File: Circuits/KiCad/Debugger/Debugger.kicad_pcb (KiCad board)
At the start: 2 copper layers, 104.1 x 104.1 mm, 11 parts, among them J1 BUS1, J2 BUS2, SW1 RESET, SW2 POWER

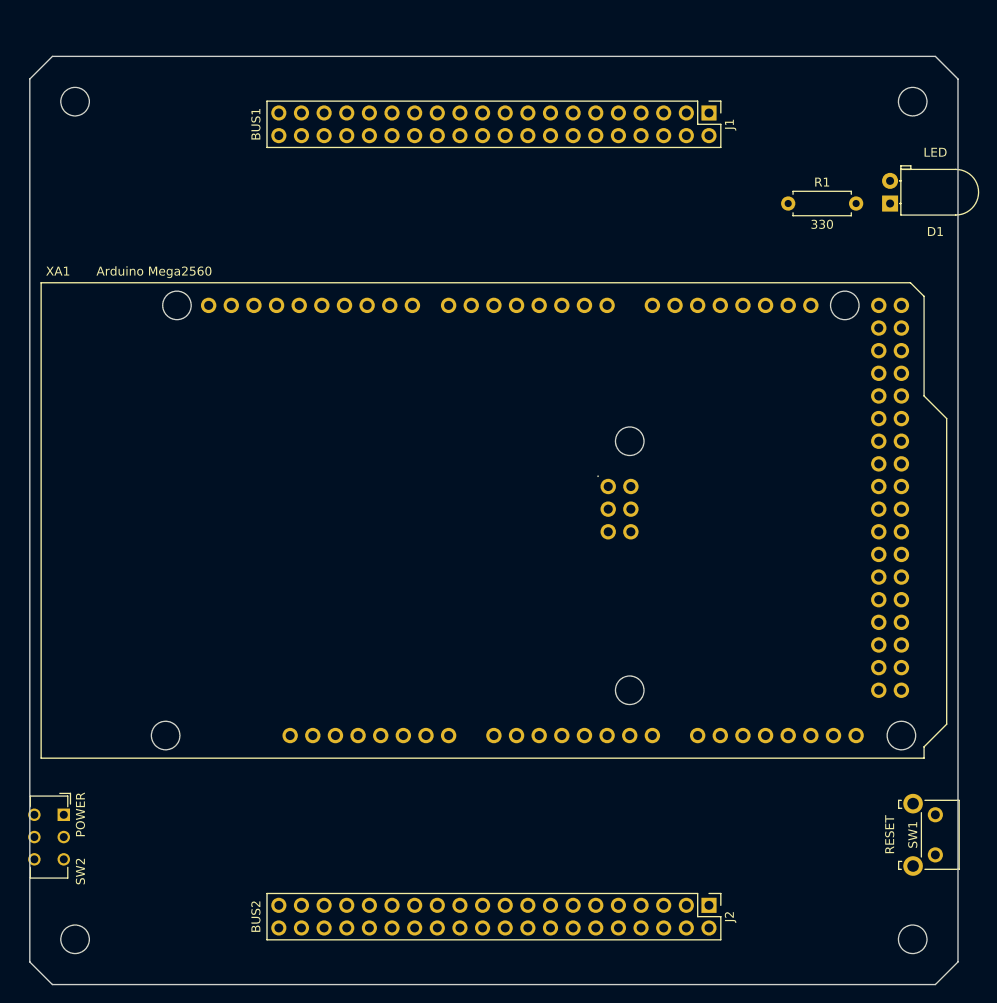
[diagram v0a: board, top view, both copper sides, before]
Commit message: Updated PCB for Bottom and Debugger (sent to manufacturer)
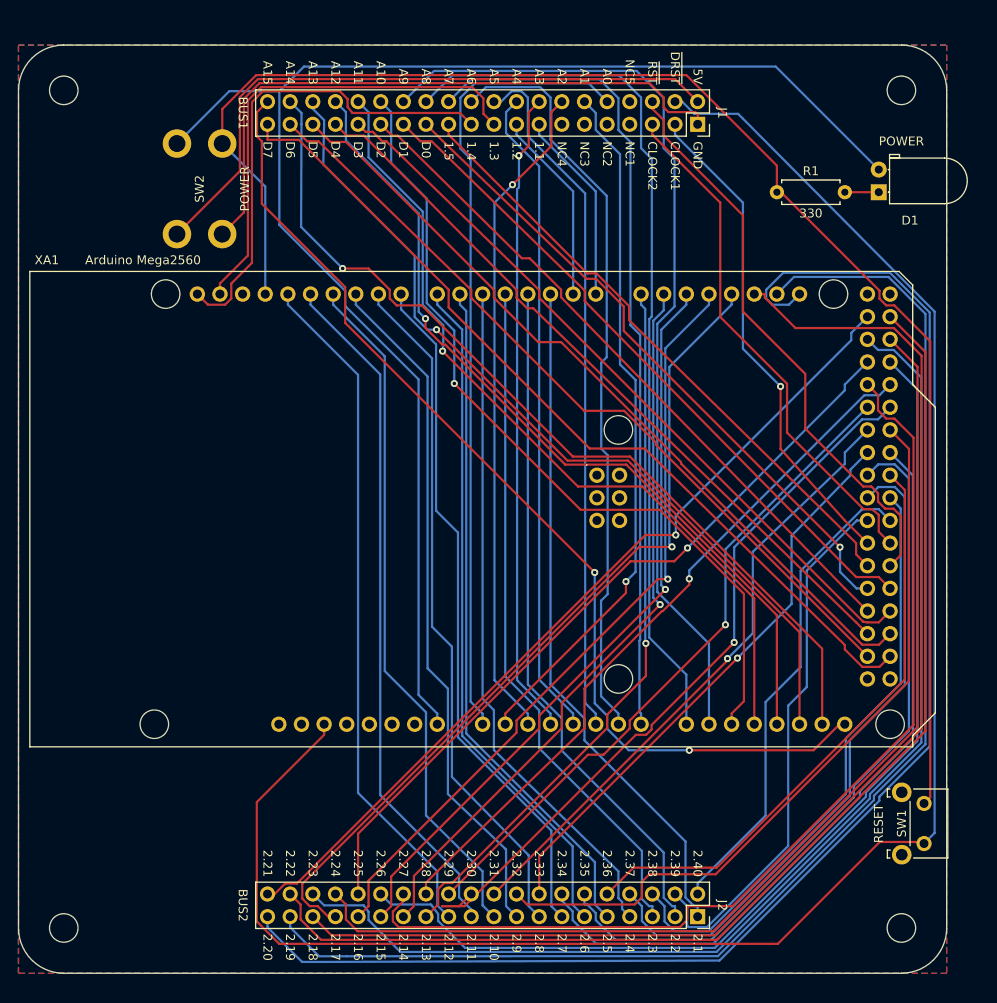
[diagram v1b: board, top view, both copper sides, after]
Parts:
- D1: value LED -> POWER
- J1, J2: footprint Connector_PinHeader_2.54mm:PinHeader_2x20_P2.54mm_Vertical -> Connector_PinSocket_2.54mm:PinSocket_2x20_P2.54mm_Vertical
- SW2: footprint Button_Switch_THT:SW_CuK_JS202011AQN_DPDT_Angled -> DM-02:Switch_DPST_Angled
- moved SW2 62.9 mm to (39.4, 49.5), turned to 90 degrees
- moved H3 1.80 mm to (124.5, 124.5)
- moved SW1 1.80 mm to (127.0, 110.5)
- moved R1 1.80 mm to (110.5, 41.9)
- moved H2 1.80 mm to (30.5, 124.5)
- moved H4 1.80 mm to (124.5, 30.5)
- moved J1 1.80 mm to (101.6, 34.3)
- moved J2 1.80 mm to (101.6, 123.2)
- moved D1 1.80 mm to (121.9, 41.9)
- moved H1 1.80 mm to (30.5, 30.5)
- moved XA1 1.80 mm to (26.7, 104.1)
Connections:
- D1 pad 2: COMPUTER_5V -> ARDUINO_5V
- J1 pad 15: Net-(J1-Pad15) -> BUS1_1
- J1 pad 17: Net-(J1-Pad17) -> BUS1_2
- J1 pad 19: Net-(J1-Pad19) -> BUS1_3
- J1 pad 21: Net-(J1-Pad21) -> BUS1_4
- J1 pad 23: Net-(J1-Pad23) -> BUS1_5
- J1 pad 3: Net-(J1-Pad3) -> CLOCK1
- J1 pad 5: Net-(J1-Pad5) -> CLOCK2
- XA1 pad D0: Net-(XA1-PadD0) -> BUS1_1
- XA1 pad D1: Net-(XA1-PadD1) -> BUS1_2
- XA1 pad D42: Net-(XA1-PadD42) -> CLOCK1
- XA1 pad D43: Net-(XA1-PadD43) -> CLOCK2
- XA1 pad D44: Net-(XA1-PadD44) -> BUS1_5
- XA1 pad SCL: Net-(XA1-PadSCL) -> BUS1_4
- XA1 pad SDA: Net-(XA1-PadSDA) -> BUS1_3
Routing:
- net ~DEBUG_RESET: track 0.00 -> 205.1 mm
- net ARDUINO_GND: track 0.00 -> 170.5 mm
- net ARDUINO_5V: track 0.00 -> 165.5 mm
- net BUS2_20: track 0.00 -> 162.5 mm
- net BUS2_19: track 0.00 -> 151.4 mm
- net BUS2_18: track 0.00 -> 142.5 mm
- net BUS2_22: track 0.00 -> 132.2 mm
- net BUS2_23: track 0.00 -> 130.4 mm
- net BUS2_24: track 0.00 -> 122.3 mm
- net BUS2_26: track 0.00 -> 116.9 mm
- net A15: track 0.00 -> 116.8 mm, vias 0 -> 2
- net BUS2_27: track 0.00 -> 113.3 mm
- net A9: track 0.00 -> 105.9 mm
- net A14: track 0.00 -> 101.7 mm, vias 0 -> 1
- net A8: track 0.00 -> 99.1 mm
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- added copper zone on B.Cu, net (none)
- added copper zone on F.Cu, net (none)
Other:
- outline, holes or cut-outs redrawn
- board text added: "1.1"
- board text added: "1.2"
- board text added: "1.3"
- board text added: "1.4"
- board text added: "1.5"
- board text added: "2.1"
- board text added: "2.10"
- board text added: "2.11"
- board text added: "2.12"
- board text added: "2.13"
- board text added: "2.14"
- board text added: "2.15"
- board text added: "2.16"
- board text added: "2.17"
- board text added: "2.18"
- board text added: "2.19"
- board text added: "2.2"
- board text added: "2.20"
- board text added: "2.21"
- board text added: "2.22"
- board text added: "2.23"
- board text added: "2.24"
- board text added: "2.25"
- board text added: "2.26"
- board text added: "2.27"
- board text added: "2.28"
- board text added: "2.29"
- board text added: "2.3"
- board text added: "2.30"
- board text added: "2.31"
- board text added: "2.32"
- board text added: "2.33"
- board text added: "2.34"
- board text added: "2.35"
- board text added: "2.36"
- board text added: "2.37"
- board text added: "2.38"
- board text added: "2.39"
- board text added: "2.4"
- board text added: "2.40"
- board text added: "2.5"
- board text added: "2.6"
- board text added: "2.7"
- board text added: "2.8"
- board text added: "2.9"
- board text added: "5V"
- board text added: "A0"
- board text added: "A1"
- board text added: "A10"
- board text added: "A11"
- board text added: "A12"
- board text added: "A13"
- board text added: "A14"
- board text added: "A15"
- board text added: "A2"
- board text added: "A3"
- board text added: "A4"
- board text added: "A5"
- board text added: "A6"
- board text added: "A7"
- board text added: "A8"
- board text added: "A9"
- board text added: "CLOCK1"
- board text added: "CLOCK2"
- board text added: "D0"
- board text added: "D1"
- board text added: "D2"
- board text added: "D3"
- board text added: "D4"
- board text added: "D5"
- board text added: "D6"
- board text added: "D7"
- board text added: "GND"
- board text added: "NC1"
- board text added: "NC2"
- board text added: "NC3"
- board text added: "NC4"
- board text added: "NC5"
- board text added: "~DRST"
- board text added: "~RST"

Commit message: Routed power & clock PCB
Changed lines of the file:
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@@
   (general
     (thickness 1.6)
-    (drawings 89)
+    (drawings 90)
     (tracks 769)
     (zones 0)
@@
   (page A4)
   (layers
-    (0 F.Cu signal hide)
+    (0 F.Cu signal)
     (31 B.Cu signal)
     (32 B.Adhes user hide)
@@
     (44 Edge.Cuts user)
     (45 Margin user)
-    (46 B.CrtYd user hide)
-    (47 F.CrtYd user hide)
+    (46 B.CrtYd user)
+    (47 F.CrtYd user)
     (48 B.Fab user hide)
-    (49 F.Fab user hide)
+    (49 F.Fab user)
   )
   (setup
@@
       (net 16 "Net-(XA1-PadMISO)"))
   )
+  (gr_poly (pts (xy 129.54 38.1) (xy 123.13 38.08) (xy 123.19 25.4) (xy 129.54 25.4)) (layer F.SilkS) (width 0.1))
   (gr_text 2.36 (at 91.44 118.745 270) (layer F.SilkS)
     (effects (font (size 1 1) (thickness 0.15)) (justify right))

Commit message: Documentation
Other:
- board text added: "DM-02 | Debugger | Revision 2"
- board text removed: "Debugger | Revision 1"
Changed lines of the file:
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@@
   (general
     (thickness 1.6)
-    (drawings 90)
+    (drawings 89)
     (tracks 769)
     (zones 0)
@@
       (effects (font (size 1 1) (thickness 0.15)))
     )
-    (fp_text value 330 (at 3.81 2.37) (layer F.SilkS)
-      (effects (font (size 1 1) (thickness 0.15)))
+    (fp_text value 330 (at 3.81 0) (layer B.SilkS)
+      (effects (font (size 1 1) (thickness 0.15)) (justify mirror))
     )
     (fp_line (start 0.66 -1.25) (end 0.66 1.25) (layer F.Fab) (width 0.1))
@@
       (net 16 "Net-(XA1-PadMISO)"))
   )
-  (gr_poly (pts (xy 129.54 38.1) (xy 123.13 38.08) (xy 123.19 25.4) (xy 129.54 25.4)) (layer F.SilkS) (width 0.1))
   (gr_text 2.36 (at 91.44 118.745 270) (layer F.SilkS)
     (effects (font (size 1 1) (thickness 0.15)) (justify right))
@@
   (gr_arc (start 30.48 124.46) (end 25.4 124.46) (angle -90) (layer Edge.Cuts) (width 0.15))
   (gr_arc (start 124.46 124.46) (end 124.46 129.54) (angle -90) (layer Edge.Cuts) (width 0.15))
-  (gr_text "Debugger | Revision 1" (at 77.47 127) (layer B.SilkS)
+  (gr_text "DM-02 | Debugger | Revision 2" (at 77.47 127) (layer B.SilkS)
     (effects (font (size 1 1) (thickness 0.1)) (justify mirror))
   )
